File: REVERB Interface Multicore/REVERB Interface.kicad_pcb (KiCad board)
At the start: 2 copper layers, 90.2 x 95.9 mm, 72 parts, among them J1 RPiZeroW, J2 Iridium, J3 APRS, J4 Antenna, J5 UPDI, M1 MountingHole_Pad, M2 MountingHole_Pad, M3 MountingHole_Pad, M4 MountingHole_Pad, M5 PiMount, M6 PiMount, M7 PiMount, M8 PiMount, U1 IMU, U2 MAX3232, U3 ATtiny1604-SS, U4 TXB0104D

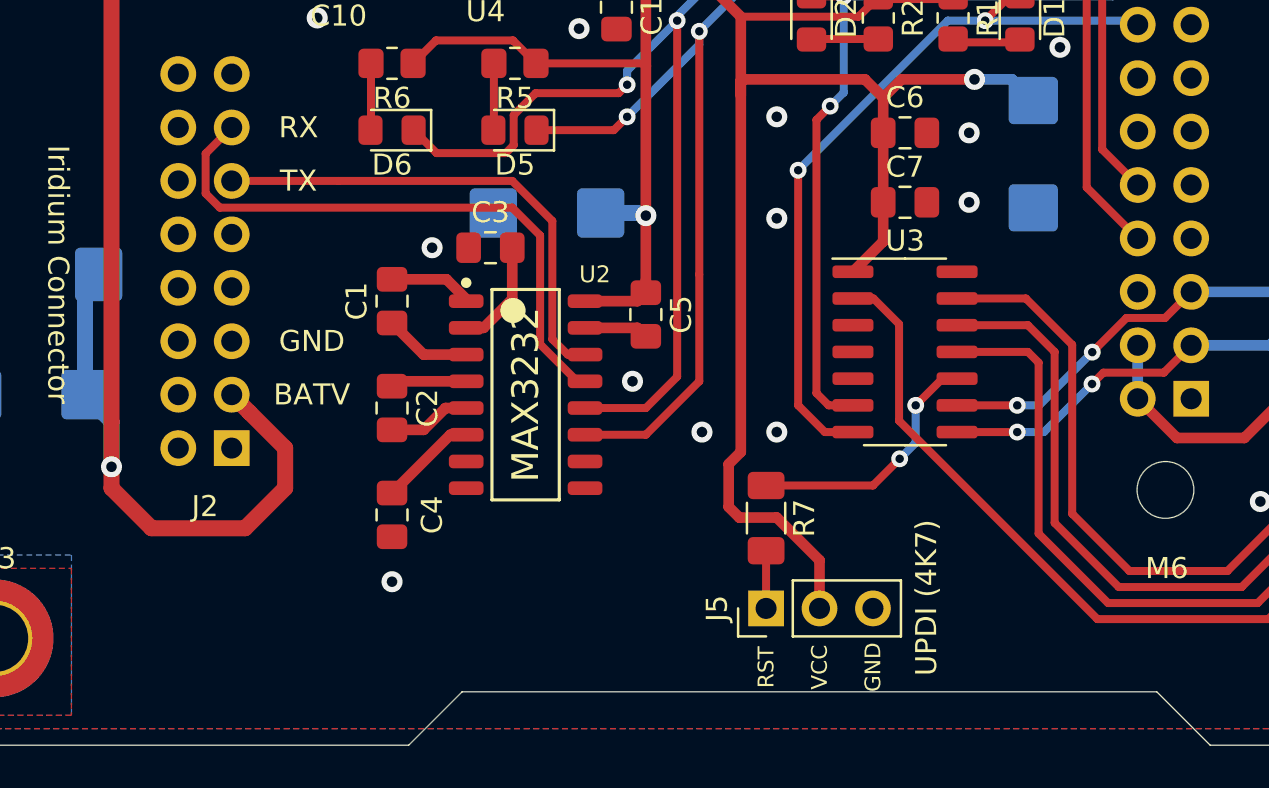
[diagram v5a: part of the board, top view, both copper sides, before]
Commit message: route, edit i2c description
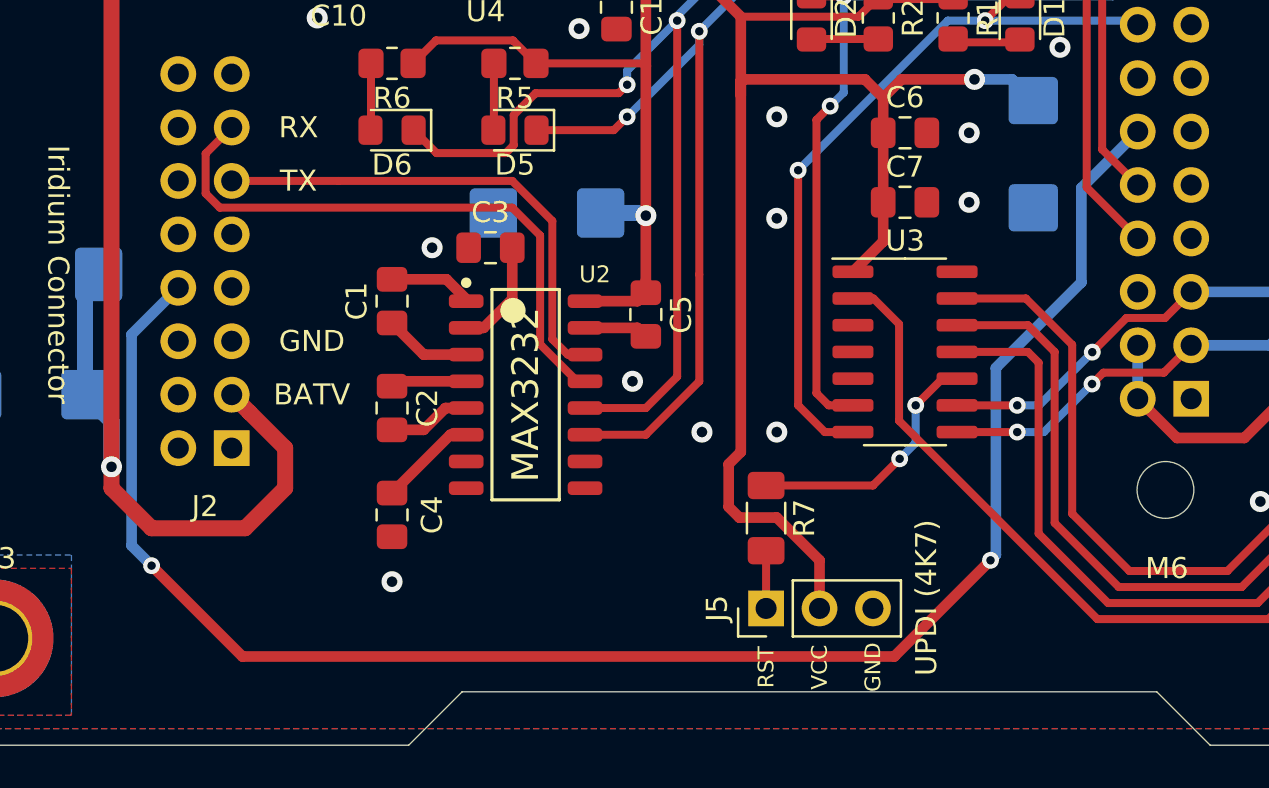
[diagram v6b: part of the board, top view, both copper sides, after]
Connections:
- J1 pad 12: (no net) -> /RI
- J2 pad 15: (no net) -> GND
- J2 pad 8: (no net) -> /RI
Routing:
- net /RI: track 0.00 -> 81.4 mm, vias 0 -> 2

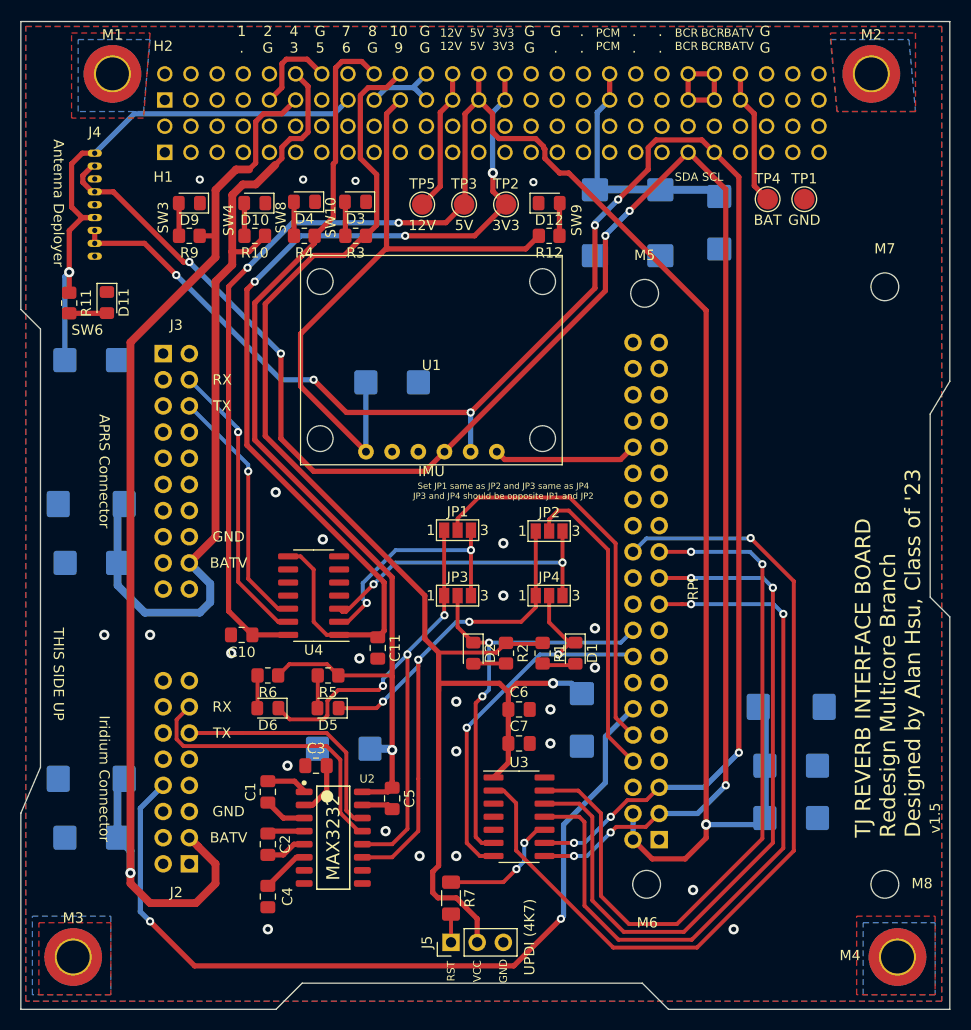
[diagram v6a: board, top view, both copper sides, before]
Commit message: implement rtc on a pdm
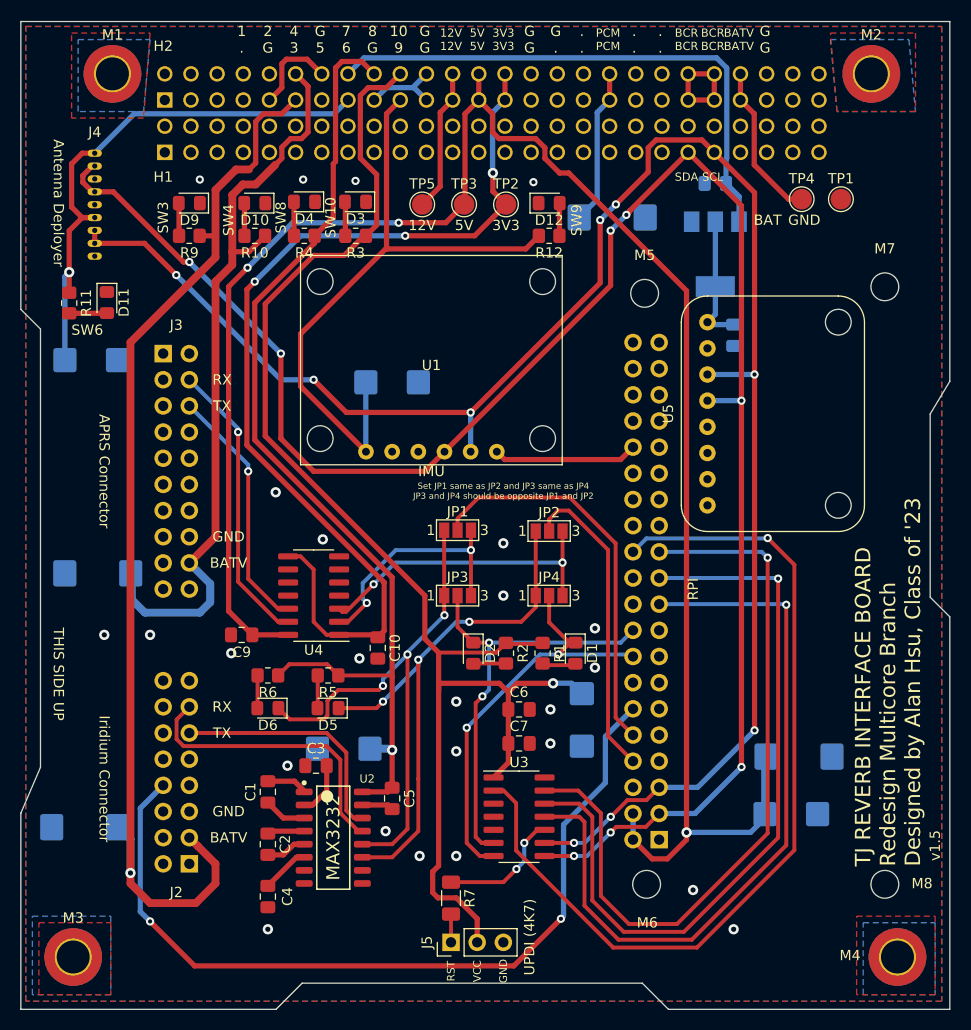
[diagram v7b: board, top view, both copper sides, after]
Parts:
- removed the C12 at (181.6, 130.2)
- removed the C14 at (113.7, 132.1)
- removed the C18 at (168.9, 72.4)
- removed the C19 at (174.6, 72.4)
- added C20: 10uF, Capacitor_SMD:C_0805_2012Metric_Pad1.18x1.45mm_HandSolder, B.Cu at (174.2, 68.6)
- added U5: DS3231BOB, REVERB Interface:DS3231BOB, F.Cu at (173.5, 90.9)
- added U6: LM1117-3.3, Package_TO_SOT_SMD:SOT-223-3_TabPin2, B.Cu at (174.2, 75.4)
- C17: renamed from C22; value 47uF -> 22uF
- C18: renamed from C16; value 47uF -> 22uF
- C19: renamed from C23; value 47uF -> 22uF
- C21: value 47uF -> 10uF; footprint Capacitor_Tantalum_SMD:CP_EIA-6032-28_Kemet-C_Pad2.25x2.35mm_HandSolder -> Capacitor_SMD:C_0805_2012Metric_Pad1.18x1.45mm_HandSolder
- moved C21 66.1 mm to (176.0, 83.3), turned to 270 degrees
- moved C15 6.76 mm to (114.3, 106.4)
- moved C11 4.89 mm to (182.4, 124.2)
- moved C14 4.74 mm to (113.0, 131.1)
- moved C13 4.70 mm to (181.6, 129.8)
- moved TP1 3.56 mm to (186.4, 70.1)
- moved TP4 3.30 mm to (182.6, 70.1)
- moved C12 1.75 mm to (164.2, 71.9), turned to 0 degrees
- renumbered C11 to C10, C8 to C11, C17 to C12, C9 to C13, C13 to C14, C20 to C15, C15 to C16, C10 to C9
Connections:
- C21 pad 1: /SW4 -> Net-(C21-Pad1)
- H2 pad 16: (no net) -> /SW7
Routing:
- net /SW7: track 0.00 -> 53.3 mm
- net Net-(C21-Pad1): track 0.00 -> 12.7 mm
- net /PCM_IN: track 24.2 -> 15.2 mm
- net /SW4: track 81.3 -> 73.7 mm
- net +5V: track 189.3 -> 183.5 mm
- net /EPSSCL: track 170.2 -> 175.6 mm, vias 8 -> 9
- net /SW3: track 111.3 -> 106.3 mm
- net /EPSSDA: track 176.8 -> 181.2 mm, vias 7 -> 8
- net VBUS: track 13.3 -> 15.4 mm
- net /SPIMISO: track 71.9 -> 73.1 mm, vias 2 -> 1
- net /SPISCK: track 71.8 -> 72.9 mm, vias 2 -> 1
- net /SPICE0: track 86.1 -> 87.1 mm
- net /SPIMOSI: track 71.7 -> 72.7 mm, vias 2 -> 1
